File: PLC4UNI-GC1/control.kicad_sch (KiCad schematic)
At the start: 13 parts, among them J1 Conn_02x07_Odd_Even, SW1 TS-1088-AR02016, U1 ESP32-S3-WROOM-1, U10 ADS1115IDGS, U4 RS485-PROTECT

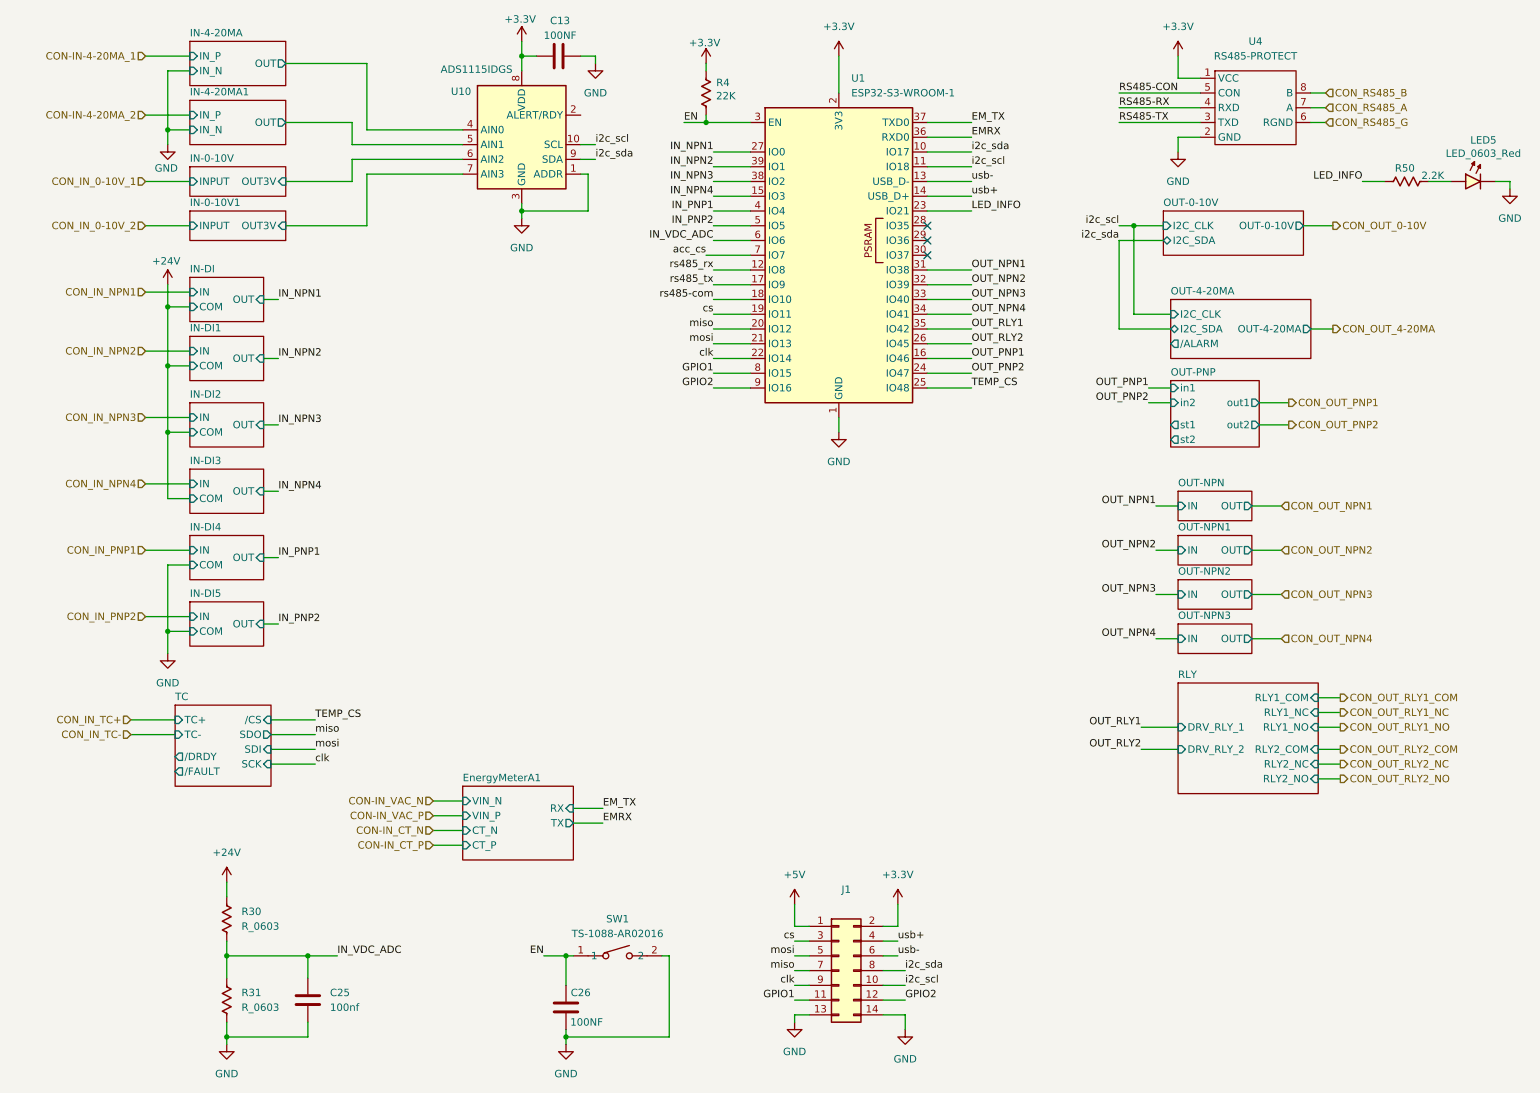
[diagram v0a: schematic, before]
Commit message: Colocadas el 80% de las piezas
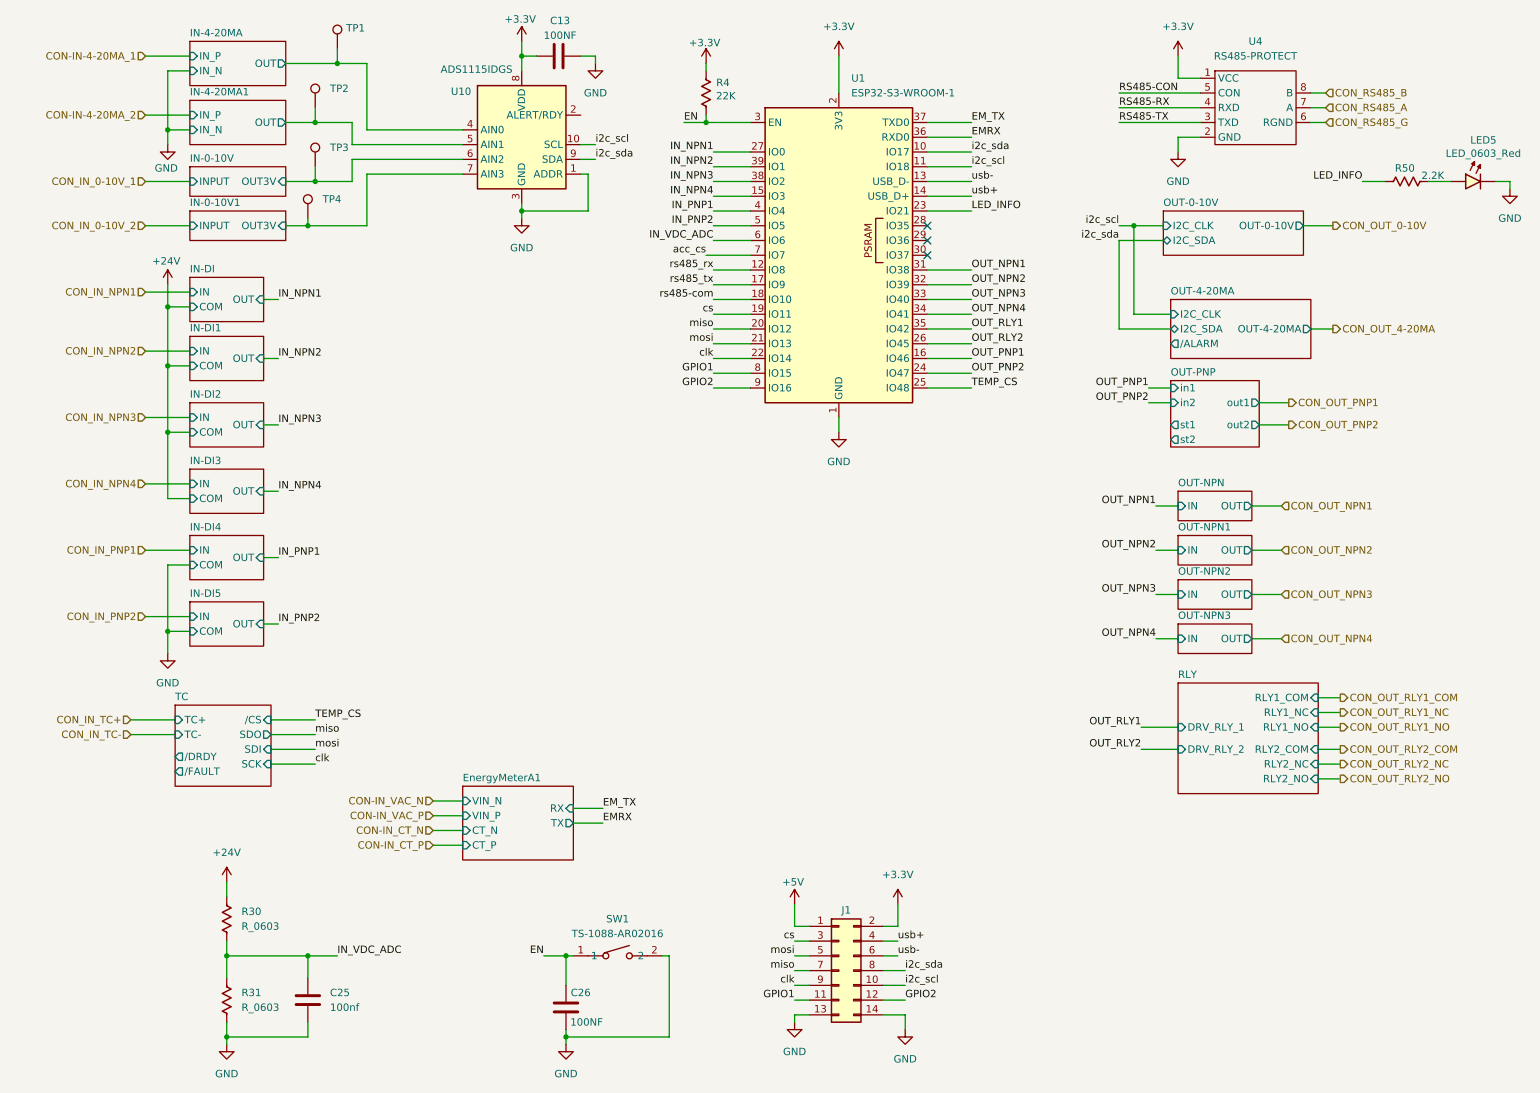
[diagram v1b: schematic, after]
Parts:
- added TP1, TP2, TP3, TP4: TestPoint_Hole1, 4ms_TestPoint:TestPoint_WireHole, symbol MG_ELECTROMECANICAL:TestPoint_Hole1
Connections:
- net IN-0-10V/OUT3V: now also TP3.1
- net IN-0-10V1/OUT3V: now also TP4.1
- net IN-4-20MA/OUT: now also TP1.1
- net IN-4-20MA1/OUT: now also TP2.1

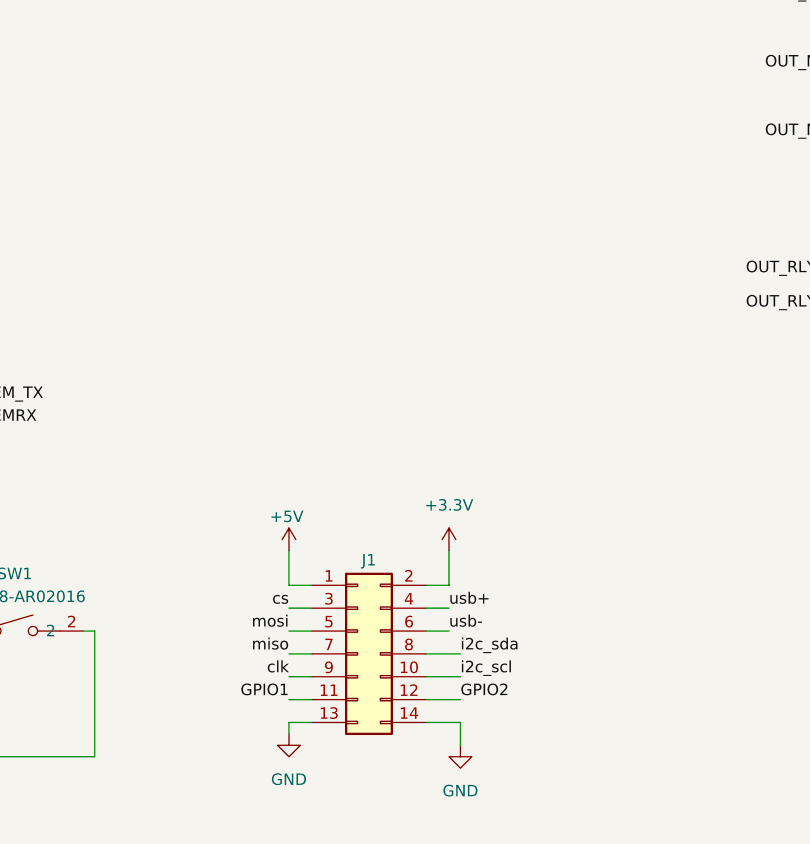
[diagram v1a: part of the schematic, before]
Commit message: Avances en colocacion de piezas y verificacion de componentes
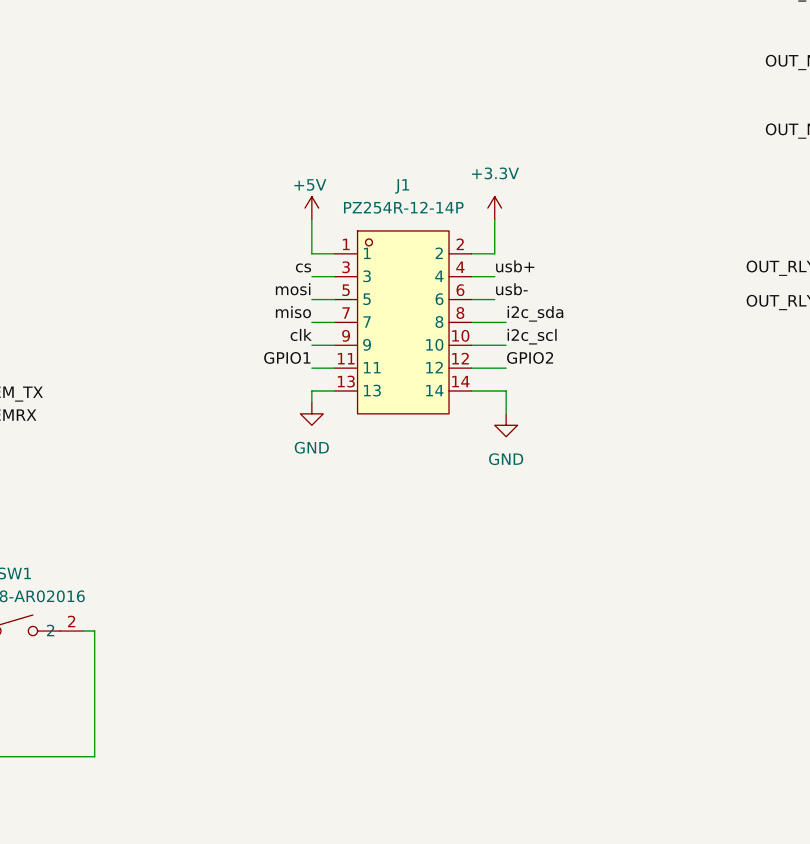
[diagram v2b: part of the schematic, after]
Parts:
- removed J1: Conn_02x07_Odd_Even, Connector_PinHeader_2.54mm:PinHeader_2x07_P2.54mm_Vertical, symbol Connector_Generic:Conn_02x07_Odd_Even
- added J1: PZ254R-12-14P, EasyEDA:HDR-TH_14P-P2.54-H-M-R2-C7-S2.54, symbol EasyEDA:PZ254R-12-14P
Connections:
- net +3.3V: now also J1.2
- net +5V: now also J1.1
- net GND: now also J1.13, J1.14
- net GPIO1: now also J1.11
- net GPIO2: now also J1.12
- net clk: now also J1.9
- net cs: now also J1.3
- net i2c_scl: now also J1.10
- net i2c_sda: now also J1.8
- net miso: now also J1.7
- net mosi: now also J1.5
- net usb+: now also J1.4
- net usb-: now also J1.6
